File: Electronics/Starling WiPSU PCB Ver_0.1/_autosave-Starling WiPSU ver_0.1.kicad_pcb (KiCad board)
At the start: 2 copper layers, 60 x 20 mm, 26 parts, among them CON1 9V/2A, P1 HC-05 Bluetooth, P2 ESP8266 - 01, P3 CONN_01X01, P4 CONN_01X01, P6 2.3" Display Conn, Q1 BSS138, Q2 BSS138, Q3 BC847, SW1 SW_PUSH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

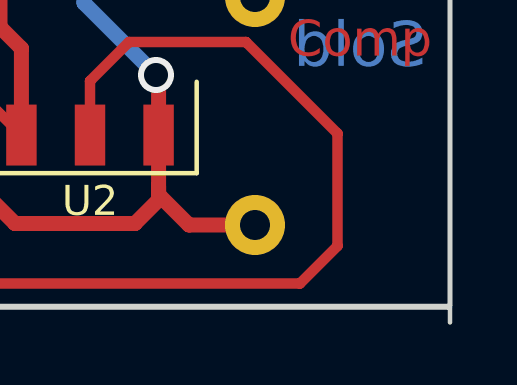
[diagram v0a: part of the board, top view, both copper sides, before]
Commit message: Wifi BO added
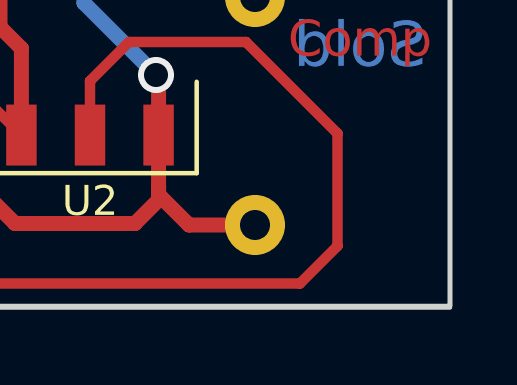
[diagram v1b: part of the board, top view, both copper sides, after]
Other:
- board size 60 x 20 mm -> 60 x 19.5 mm
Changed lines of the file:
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@@
     (links 55)
     (no_connects 6)
-    (area 84.891667 74.375 150.989286 101.525)
+    (area 84.891667 74.375 210.989286 121.075)
     (thickness 1.6)
-    (drawings 11)
+    (drawings 10)
     (tracks 224)
     (zones 0)
@@
     (pad "" np_thru_hole circle (at 0 0) (size 3.2 3.2) (drill 3) (layers *.Cu *.Mask F.SilkS))
   )
+  (gr_line (start 146 96.55) (end 86 96.55) (angle 90) (layer Edge.Cuts) (width 0.15))
+  (gr_line (start 86 96.5) (end 146 96.5) (angle 90) (layer Edge.Cuts) (width 0.15))
   (gr_line (start 146 77) (end 146 96.5) (angle 90) (layer Edge.Cuts) (width 0.15))
-  (gr_line (start 146 97.05) (end 146 96.55) (angle 90) (layer Edge.Cuts) (width 0.15))
-  (gr_line (start 146 96.55) (end 86 96.55) (angle 90) (layer Edge.Cuts) (width 0.15))
   (gr_text Sold (at 143 87.8) (layer B.Cu)
     (effects (font (size 1.5 1.5) (thickness 0.3)) (justify mirror))
@@
   )
   (gr_line (start 146 96.5) (end 146 77.5) (angle 90) (layer Edge.Cuts) (width 0.15))
-  (gr_line (start 86 96.5) (end 146 96.5) (angle 90) (layer Edge.Cuts) (width 0.15))
   (gr_line (start 86 77) (end 86 96.5) (angle 90) (layer Edge.Cuts) (width 0.15))
   (gr_line (start 146 77) (end 86 77) (angle 90) (layer Edge.Cuts) (width 0.15))
